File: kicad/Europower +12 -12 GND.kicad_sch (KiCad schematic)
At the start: 10 parts, among them J9 Conn_02x05_Odd_Even

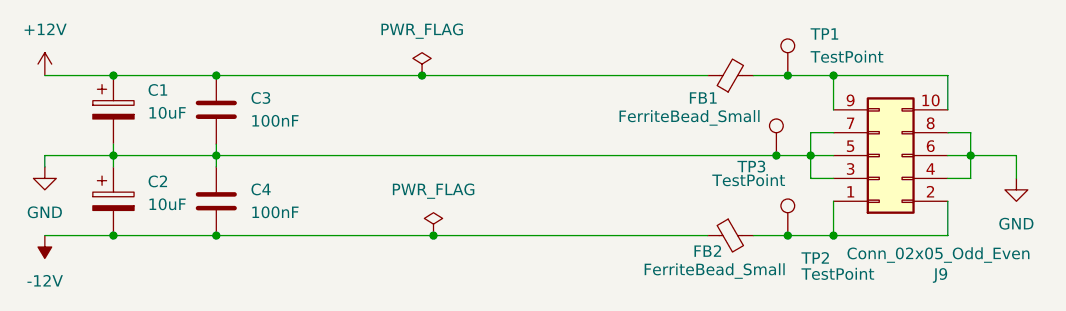
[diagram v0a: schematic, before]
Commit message: Refactor KiCad project files for improved layout and organization
- Adjusted column widths in buffer-module.kicad_prl for better readability.
- Cleared unnecessary DRC exclusions in buffer-module.kicad_pro to streamline design rules.
- Updated sheet positions and properties in buffer-module.kicad_sch for enhanced clarity.
- Realigned junctions and wires in quad buffer schematic for improved circuit flow and readability.
- Corrected component positions and properties in quad buffer schematic to ensure accurate representation.
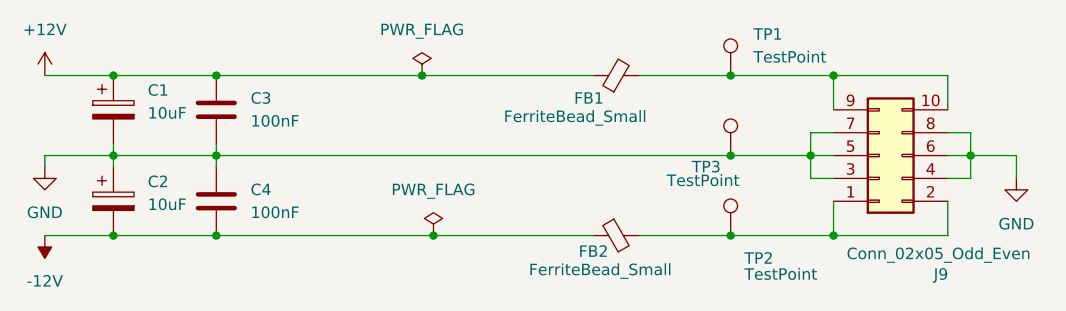
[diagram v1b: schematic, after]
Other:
- moved on the sheet: FB1, FB2, TP1, TP2, TP3
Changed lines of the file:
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@@
-	)
-	(junction
-		(at 171.45 92.71)
-		(diameter 0)
-		(color 0 0 0 0)
 	)
 	(junction
@@
 	)
 	(junction
-		(at 170.18 101.6)
-		(diameter 0)
-		(color 0 0 0 0)
-	)
-	(junction
 		(at 176.53 92.71)
 		(diameter 0)
@@
 	)
 	(junction
+		(at 165.1 101.6)
+		(diameter 0)
+		(color 0 0 0 0)
+	)
+	(junction
 		(at 132.08 110.49)
+		(diameter 0)
+		(color 0 0 0 0)
+	)
+	(junction
+		(at 165.1 110.49)
 		(diameter 0)
 		(color 0 0 0 0)
@@
 	)
 	(junction
-		(at 171.45 110.49)
+		(at 165.1 92.71)
 		(diameter 0)
 		(color 0 0 0 0)
@@
 	(wire
 		(pts
-			(xy 171.45 110.49) (xy 176.53 110.49)
-		)
-		(stroke
-			(width 0)
-			(type default)
-		)
-	)
-	(wire
-		(pts
 			(xy 107.95 92.71) (xy 130.81 92.71)
 		)
@@
 	(wire
 		(pts
-			(xy 107.95 101.6) (xy 170.18 101.6)
+			(xy 107.95 101.6) (xy 165.1 101.6)
 		)
 		(stroke
@@
 	(wire
 		(pts
-			(xy 132.08 110.49) (xy 162.56 110.49)
+			(xy 132.08 110.49) (xy 149.86 110.49)
+		)
+		(stroke
+			(width 0)
+			(type default)
+		)
+	)
+	(wire
+		(pts
+			(xy 165.1 101.6) (xy 173.99 101.6)
 		)
 		(stroke
@@
 	(wire
 		(pts
-			(xy 167.64 110.49) (xy 171.45 110.49)
+			(xy 154.94 110.49) (xy 165.1 110.49)
 		)
 		(stroke
@@
 	(wire
 		(pts
+			(xy 165.1 110.49) (xy 176.53 110.49)
+		)
+		(stroke
+			(width 0)
+			(type default)
+		)
+	)
+	(wire
+		(pts
 			(xy 191.77 101.6) (xy 196.85 101.6)
 		)
@@
 	(wire
 		(pts
-			(xy 170.18 101.6) (xy 173.99 101.6)
-		)
-		(stroke
-			(width 0)
-			(type default)
-		)
-	)
-	(wire
-		(pts
 			(xy 176.53 92.71) (xy 189.23 92.71)
 		)
@@
 	(wire
 		(pts
-			(xy 130.81 92.71) (xy 162.56 92.71)
+			(xy 130.81 92.71) (xy 149.86 92.71)
 		)
 		(stroke
@@
 	(wire
 		(pts
-			(xy 167.64 92.71) (xy 171.45 92.71)
+			(xy 154.94 92.71) (xy 165.1 92.71)
 		)
 		(stroke
@@
 	(wire
 		(pts
+			(xy 165.1 92.71) (xy 176.53 92.71)
+		)
+		(stroke
+			(width 0)
+			(type default)
+		)
+	)
+	(wire
+		(pts
 			(xy 107.95 100.33) (xy 107.95 101.6)
 		)
@@
 		(pts
 			(xy 96.52 102.87) (xy 96.52 101.6)
-		)
-		(stroke
-			(width 0)
-			(type default)
-		)
-	)
-	(wire
-		(pts
-			(xy 171.45 92.71) (xy 176.53 92.71)
 		)
 		(stroke
@@
 	(symbol
 		(lib_id "Device:FerriteBead_Small")
-		(at 165.1 92.71 90)
+		(at 152.4 92.71 90)
 		(unit 1)
 		(exclude_from_sim no)
@@
 		(dnp no)
 		(property "Reference" "FB1"
-			(at 162.052 95.25 90)
+			(at 149.352 95.25 90)
 			(effects
 				(font
@@
 		)
 		(property "Value" "FerriteBead_Small"
-			(at 160.528 97.282 90)
+			(at 147.828 97.282 90)
 			(effects
 				(font
@@
 		)
 		(property "Footprint" "Inductor_SMD:L_0805_2012Metric_Pad1.05x1.20mm_HandSolder"
-			(at 165.1 94.488 90)
+			(at 152.4 94.488 90)
 			(effects
 				(font
@@
 		)
 		(property "Datasheet" "https://www.taydaelectronics.com/datasheets/files/A-3191.PDF"
-			(at 165.1 92.71 0)
+			(at 152.4 92.71 0)
 			(effects
 				(font
@@
 		)
 		(property "Description" "Ferrite bead, small symbol"
-			(at 165.1 92.71 0)
+			(at 152.4 92.71 0)
 			(effects
 				(font
@@
 	(symbol
 		(lib_id "Connector:TestPoint")
-		(at 170.18 101.6 0)
+		(at 165.1 101.6 0)
 		(unit 1)
 		(exclude_from_sim no)
@@
 		(dnp no)
 		(property "Reference" "TP3"
-			(at 165.862 102.87 0)
+			(at 160.782 102.87 0)
 			(effects
 				(font
@@
 		)
 		(property "Value" "TestPoint"
-			(at 163.068 104.394 0)
+			(at 157.988 104.394 0)
 			(effects
 				(font
@@
 		)
 		(property "Footprint" "TestPoint:TestPoint_Pad_D1.5mm"
-			(at 175.26 101.6 0)
+			(at 170.18 101.6 0)
 			(effects
 				(font
@@
 		)
 		(property "Datasheet" "~"
-			(at 175.26 101.6 0)
+			(at 170.18 101.6 0)
 			(effects
 				(font
@@
 		)
 		(property "Description" "test point"
-			(at 170.18 101.6 0)
+			(at 165.1 101.6 0)
 			(effects
 				(font
@@
 	(symbol
 		(lib_id "Connector:TestPoint")
-		(at 171.45 92.71 0)
+		(at 165.1 92.71 0)
 		(unit 1)
 		(exclude_from_sim no)
@@
 		(fields_autoplaced yes)
 		(property "Reference" "TP1"
-			(at 173.99 88.1379 0)
+			(at 167.64 88.1379 0)
 			(effects
 				(font
@@
 		)
 		(property "Value" "TestPoint"
-			(at 173.99 90.6779 0)
+			(at 167.64 90.6779 0)
 			(effects
 				(font
@@
 		)
 		(property "Footprint" "TestPoint:TestPoint_Pad_D1.5mm"
-			(at 176.53 92.71 0)
+			(at 170.18 92.71 0)
 			(effects
 				(font
@@
 		)
 		(property "Datasheet" "~"
-			(at 176.53 92.71 0)
+			(at 170.18 92.71 0)
 			(effects
 				(font
@@
 		)
 		(property "Description" "test point"
-			(at 171.45 92.71 0)
+			(at 165.1 92.71 0)
 			(effects
 				(font
@@
 	(symbol
 		(lib_id "Device:FerriteBead_Small")
-		(at 165.1 110.49 90)
+		(at 152.4 110.49 90)
 		(mirror x)
 		(unit 1)
@@
 		(dnp no)
 		(property "Reference" "FB2"
-			(at 162.56 112.268 90)
+			(at 149.86 112.268 90)
 			(effects
 				(font
@@
 		)
 		(property "Value" "FerriteBead_Small"
-			(at 163.322 114.3 90)
+			(at 150.622 114.3 90)
 			(effects
 				(font
@@
 		)
 		(property "Footprint" "Inductor_SMD:L_0805_2012Metric_Pad1.05x1.20mm_HandSolder"
-			(at 165.1 108.712 90)
+			(at 152.4 108.712 90)
 			(effects
 				(font
@@
 		)
 		(property "Datasheet" "https://www.taydaelectronics.com/datasheets/files/A-3191.PDF"
-			(at 165.1 110.49 0)
+			(at 152.4 110.49 0)
 			(effects
 				(font
@@
 		)
 		(property "Description" "Ferrite bead, small symbol"
-			(at 165.1 110.49 0)
+			(at 152.4 110.49 0)
 			(effects
 				(font
@@
 	(symbol
 		(lib_id "Connector:TestPoint")
-		(at 171.45 110.49 0)
+		(at 165.1 110.49 0)
 		(unit 1)
 		(exclude_from_sim no)
@@
 		(dnp no)
 		(property "Reference" "TP2"
-			(at 172.974 113.03 0)
+			(at 166.624 113.03 0)
 			(effects
 				(font
@@
 		)
 		(property "Value" "TestPoint"
-			(at 172.974 114.808 0)
+			(at 166.624 114.808 0)
 			(effects
 				(font
@@
 		)
 		(property "Footprint" "TestPoint:TestPoint_Pad_D1.5mm"
-			(at 176.53 110.49 0)
+			(at 170.18 110.49 0)
 			(effects
 				(font
@@
 		)
 		(property "Datasheet" "~"
-			(at 176.53 110.49 0)
+			(at 170.18 110.49 0)
 			(effects
 				(font
@@
 		)
 		(property "Description" "test point"
-			(at 171.45 110.49 0)
-			(effects
-				(font
+			(at 165.1 110.49 0)
+			(effects
+				(font
